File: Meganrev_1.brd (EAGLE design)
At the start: 160 x 100 mm, 1 part

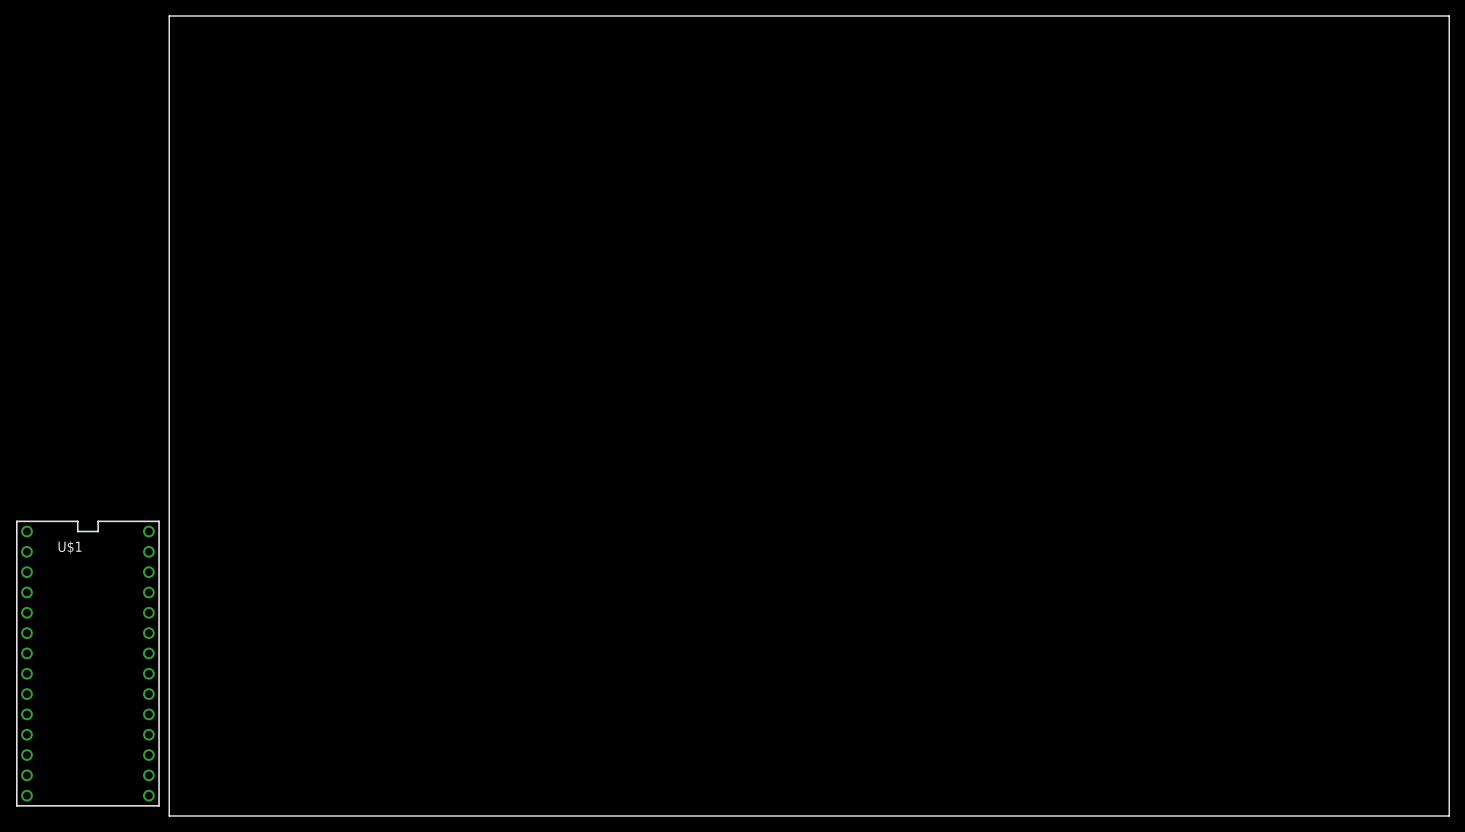
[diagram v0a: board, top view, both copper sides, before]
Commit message: create new branch for Megan's PCB
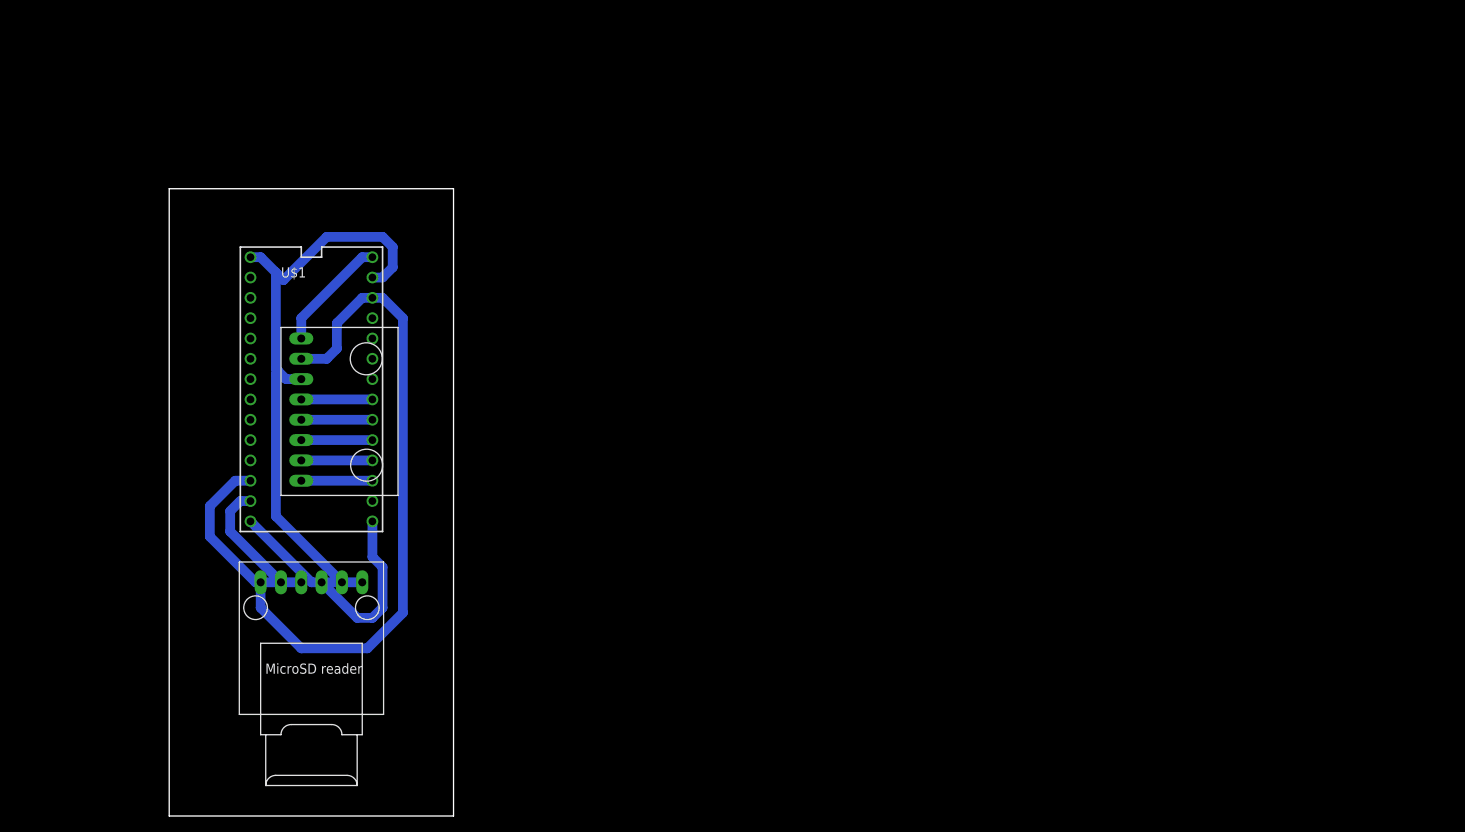
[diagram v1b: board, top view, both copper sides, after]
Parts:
- added U$2: SD_CARD_READER, macrocketry_2019:MICRO_SD_READER_3V3
- added U$3: GY-91, macrocketry_2019:GY-91
- moved U$1 44.2 mm to (17.8, 53.3)
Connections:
- removed net 3.3V: U$1.3.3V
- removed net GND: U$1.AGND, U$1.GND
- removed net VIN: U$1.VIN
- new net N$1: U$1.19/A5, U$3.SCL
- new net N$10: U$1.16/A2, U$3.NCS
- new net N$11: U$1.10, U$2.CS
- new net N$12: U$1.15/A1, U$3.CSB
- new net N$13: U$1.3.3V, U$2.3V3, U$3.3V3
- new net N$2: U$1.AGND, U$1.GND, U$2.GND, U$3.GND
- new net N$3: U$1.12, U$2.MISO
- new net N$4: U$1.11, U$2.MOSI
- new net N$5: U$1.13, U$2.CLK
- new net N$6: U$1.VIN, U$3.VIN
- new net N$8: U$1.18/A4, U$3.SDA
- new net N$9: U$1.17/A3, U$3.SAO
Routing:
- net N$13: track 0.00 -> 80.5 mm
- net N$2: track 0.00 -> 75.5 mm
- net N$11: track 0.00 -> 21.5 mm
- net N$5: track 0.00 -> 21.3 mm
- net N$4: track 0.00 -> 17.1 mm
- net N$3: track 0.00 -> 14.6 mm
- net N$6: track 0.00 -> 14.6 mm
- net N$9: track 0.00 -> 8.89 mm
- net N$8: track 0.00 -> 8.89 mm
- net N$12: track 0.00 -> 8.89 mm
- net N$10: track 0.00 -> 8.89 mm
- net N$1: track 0.00 -> 8.89 mm
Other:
- board size 160 x 100 mm -> 35.5 x 78.4 mm

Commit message: update GY-91 nameing to 10DOF-GY-91
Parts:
- U$3: value GY-91 -> 10DOF-GY91; device macrocketry_2019:GY-91 -> macrocketry_2019:10DOF-GY-91
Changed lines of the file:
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@@
 </element>
 <element name="U$2" library="macrocketry_2019" package="MICRO_SD_READER_3V3" value="SD_CARD_READER" x="17.78" y="24.13" smashed="yes" rot="R90"/>
-<element name="U$3" library="macrocketry_2019" package="GY-91" value="GY-91" x="20.32" y="52.07" smashed="yes"/>
+<element name="U$3" library="macrocketry_2019" package="10DOF-GY-91" value="10DOF-GY91" x="20.32" y="52.07" smashed="yes"/>
 </elements>
 <signals>
